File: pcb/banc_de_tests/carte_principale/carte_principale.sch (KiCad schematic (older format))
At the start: 24 parts, among them J1 Arduino_UNO_R3, J2 Conn_02x10_Odd_Even, J3 Conn_01x02, U1 AMS1117-3.3, U2 TSV911AILT

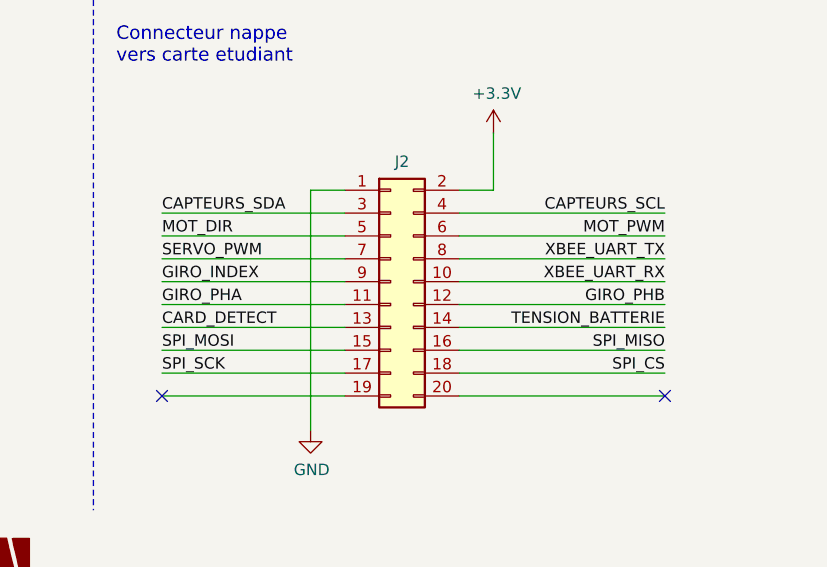
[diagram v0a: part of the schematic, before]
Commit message: Ajout du bus SPI
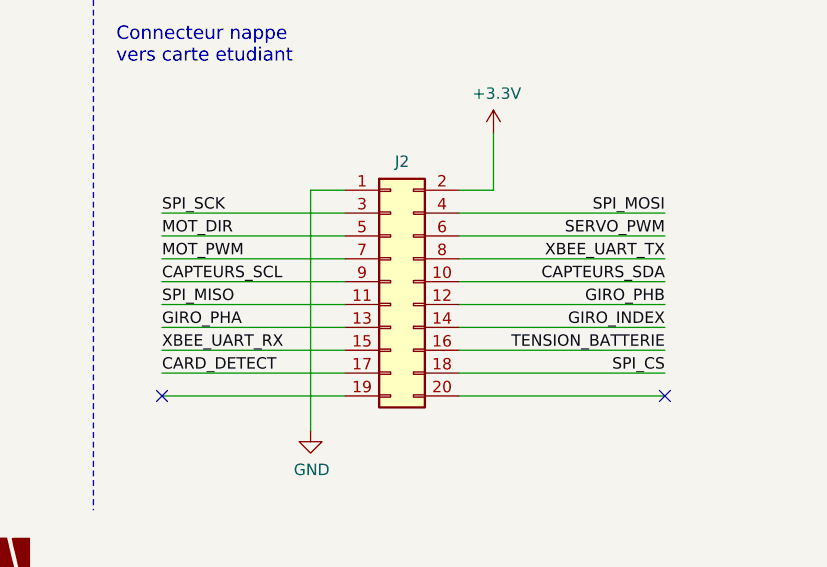
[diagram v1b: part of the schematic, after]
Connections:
- net CAPTEURS_SCL: now also J2.9 (Pin_9); no longer J2.4 (Pin_4)
- net CAPTEURS_SDA: now also J2.10 (Pin_10); no longer J2.3 (Pin_3)
- net CARD_DETECT: now also J2.17 (Pin_17); no longer J2.13 (Pin_13)
- net GIRO_INDEX: now also J2.14 (Pin_14); no longer J2.9 (Pin_9)
- net GIRO_PHA: now also J2.13 (Pin_13); no longer J2.11 (Pin_11)
- net MOT_PWM: now also J2.7 (Pin_7); no longer J2.6 (Pin_6)
- net SERVO_PWM: now also J2.6 (Pin_6); no longer J2.7 (Pin_7)
- net SPI_MISO: now also J2.11 (Pin_11); no longer J2.16 (Pin_16)
- net SPI_MOSI: now also J2.4 (Pin_4); no longer J2.15 (Pin_15)
- net SPI_SCK: now also J2.3 (Pin_3); no longer J2.17 (Pin_17)
- net TENSION_BATTERIE: now also J2.16 (Pin_16); no longer J2.14 (Pin_14)
- net XBEE_UART_RX: now also J2.15 (Pin_15); no longer J2.10 (Pin_10)
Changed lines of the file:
@@
 	1    0    0    -1
 $EndComp
-Text Label 10900 5300 2    50   ~ 0
+Text Label 8700 5400 0    50   ~ 0
 MOT_PWM
 Text Label 8700 5300 0    50   ~ 0
 MOT_DIR
-Text Label 8700 5400 0    50   ~ 0
+Text Label 10900 5300 2    50   ~ 0
 SERVO_PWM
-Text Label 8700 5600 0    50   ~ 0
+Text Label 8700 5700 0    50   ~ 0
 GIRO_PHA
 Text Label 10900 5600 2    50   ~ 0
 GIRO_PHB
+Text Label 10900 5700 2    50   ~ 0
+GIRO_INDEX
+Text Label 10900 5500 2    50   ~ 0
+CAPTEURS_SDA
 Text Label 8700 5500 0    50   ~ 0
-GIRO_INDEX
-Text Label 8700 5200 0    50   ~ 0
-CAPTEURS_SDA
-Text Label 10900 5200 2    50   ~ 0
 CAPTEURS_SCL
 Text Label 10900 5400 2    50   ~ 0
 XBEE_UART_TX
-Text Label 10900 5500 2    50   ~ 0
+Text Label 8700 5800 0    50   ~ 0
 XBEE_UART_RX
 Wire Wire Line
 	9500 5700 8700 5700
-Text Label 10900 5700 2    50   ~ 0
+Text Label 10900 5800 2    50   ~ 0
 TENSION_BATTERIE
 Wire Wire Line
@@
 Wire Wire Line
 	10000 5700 10900 5700
-Text Label 8700 5700 0    50   ~ 0
+Text Label 8700 5900 0    50   ~ 0
 CARD_DETECT
 Wire Wire Line
@@
 NoConn ~ 10900 6000
 NoConn ~ 8700 6000
-Text Label 8700 5800 0    50   ~ 0
+Text Label 10900 5200 2    50   ~ 0
 SPI_MOSI
-Text Label 8700 5900 0    50   ~ 0
+Text Label 8700 5200 0    50   ~ 0
 SPI_SCK
-Text Label 10900 5800 2    50   ~ 0
+Text Label 8700 5600 0    50   ~ 0
 SPI_MISO
 Text Label 10900 5900 2    50   ~ 0

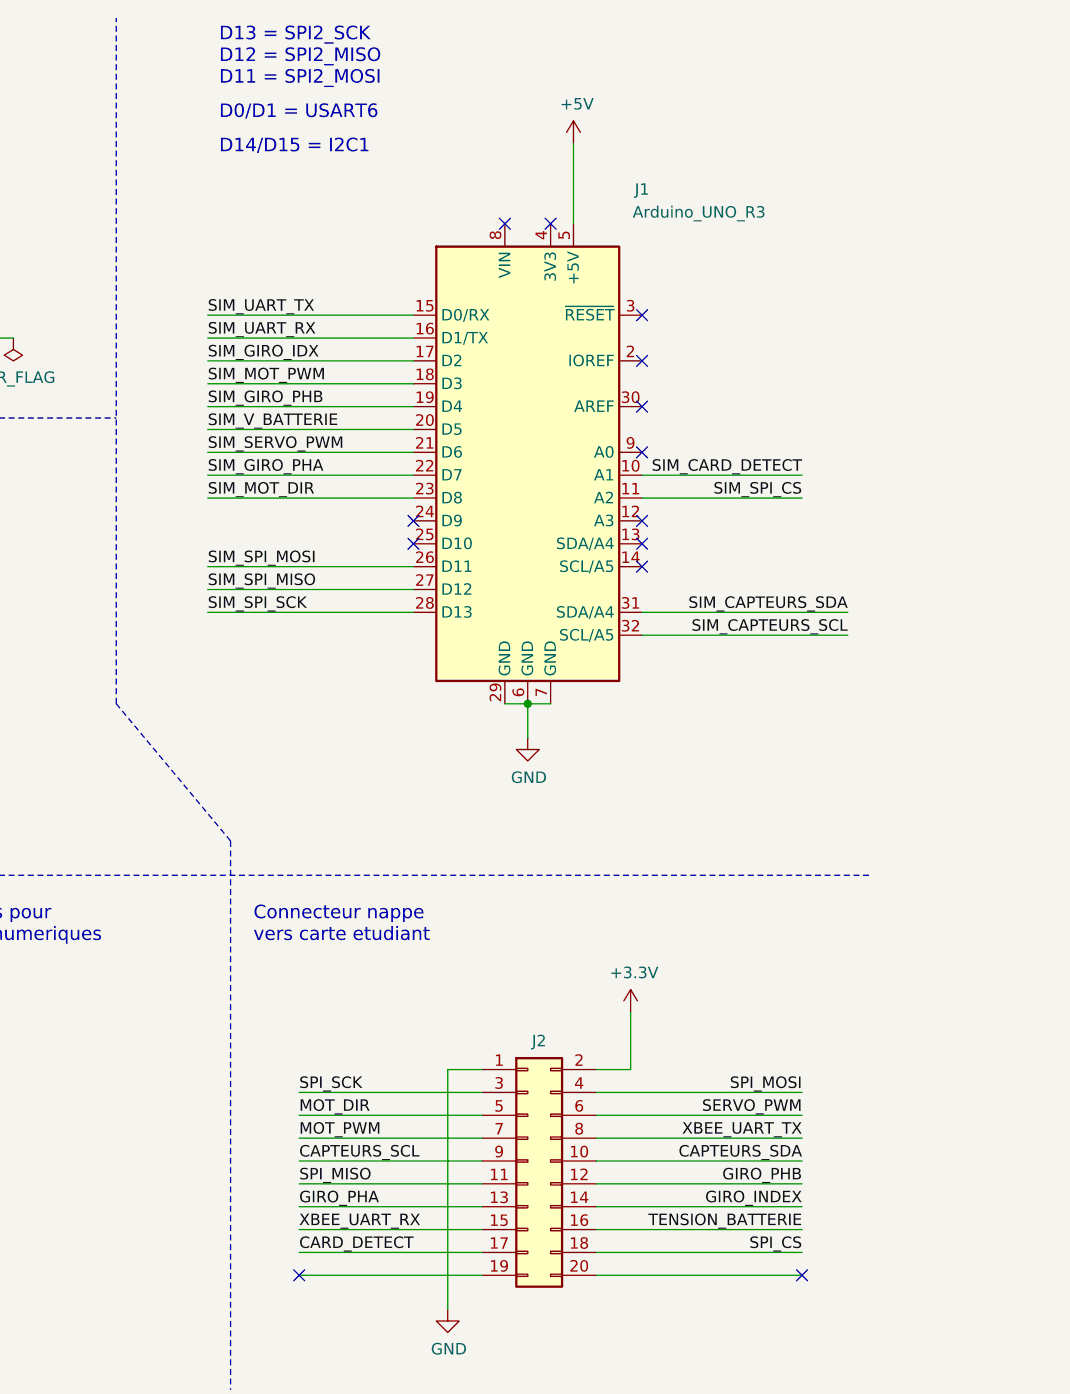
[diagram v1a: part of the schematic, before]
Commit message: * Reorganisation du connecteur de la carte etudiant * premiere version de la carte principale du banc de test * premiere version de la carte vers le connecteur de la carte etudiant
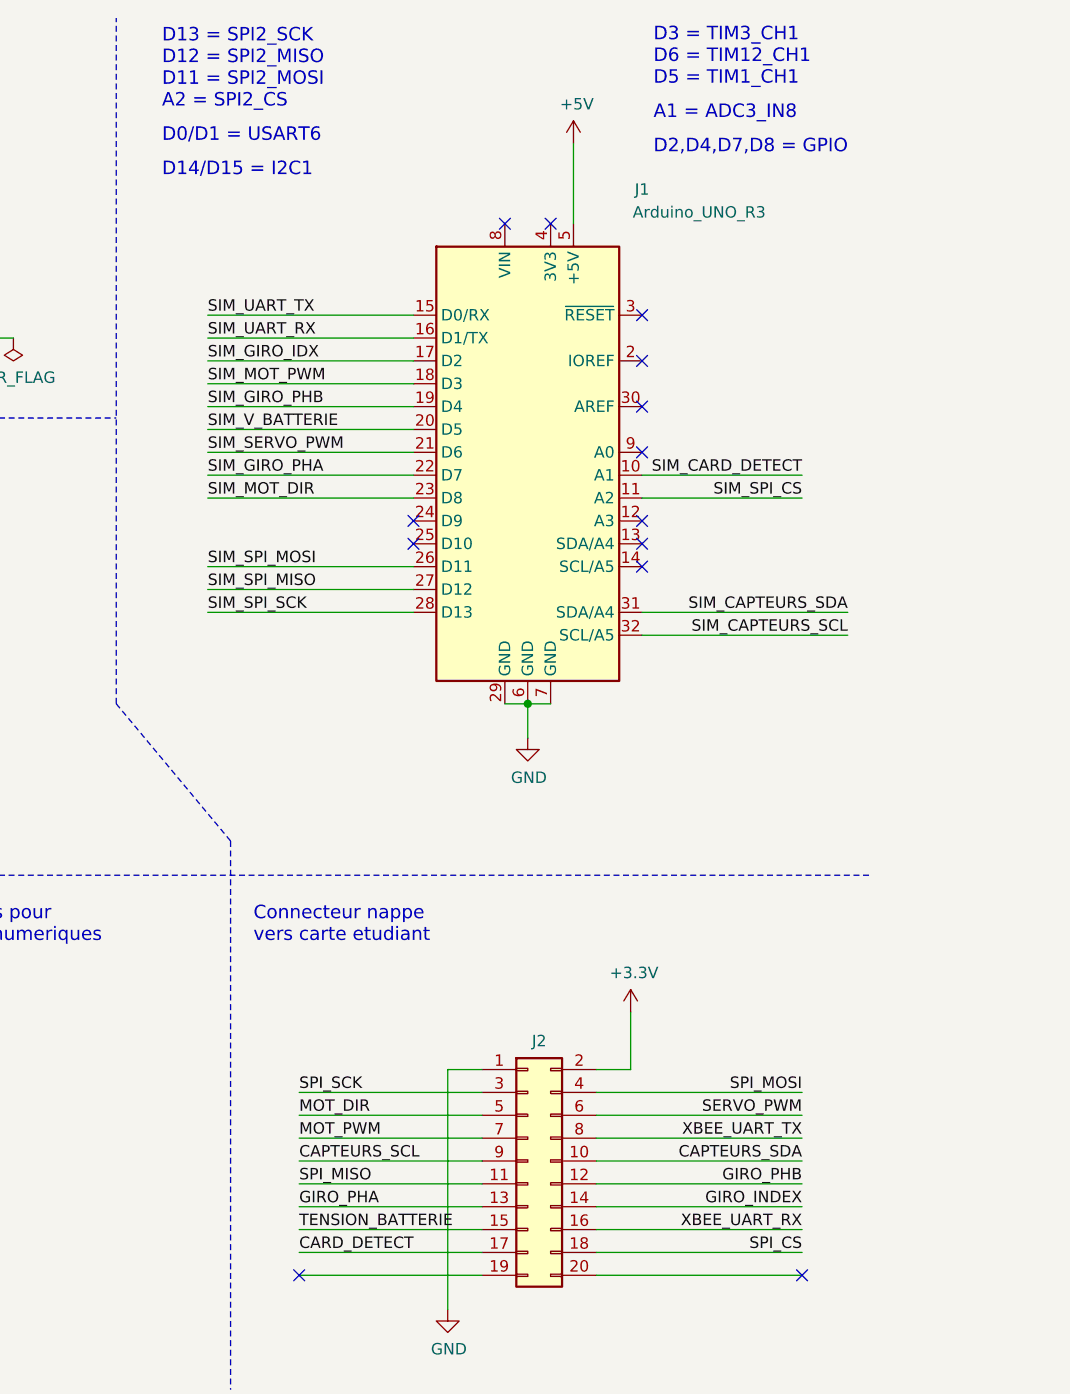
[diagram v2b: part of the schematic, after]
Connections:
- net TENSION_BATTERIE: now also J2.15 (Pin_15); no longer J2.16 (Pin_16)
- net XBEE_UART_RX: now also J2.16 (Pin_16); no longer J2.15 (Pin_15)
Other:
- note added: "A1 = ADC3_IN8"
- note added: "D13 = SPI2_SCK\nD12 = SPI2_MISO\nD11 = SPI2_MOSI\nA2 = SPI2_CS"
- note added: "D2,D4,D7,D8 = GPIO"
- note added: "D3 = TIM3_CH1\nD6 = TIM12_CH1\nD5 = TIM1_CH1"
- note removed: "D13 = SPI2_SCK\nD12 = SPI2_MISO\nD11 = SPI2_MOSI"
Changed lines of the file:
@@
 Wire Notes Line
 	7900 3500 7900 500
-Text Notes 8350 800  0    59   ~ 0
-D13 = SPI2_SCK\nD12 = SPI2_MISO\nD11 = SPI2_MOSI
-Text Notes 8350 950  0    59   ~ 0
+Text Notes 8100 900  0    59   ~ 0
+D13 = SPI2_SCK\nD12 = SPI2_MISO\nD11 = SPI2_MOSI\nA2 = SPI2_CS
+Text Notes 8100 1050 0    59   ~ 0
 D0/D1 = USART6
-Text Notes 8350 1100 0    59   ~ 0
+Text Notes 8100 1200 0    59   ~ 0
 D14/D15 = I2C1
 $Comp
@@
 Text Label 10900 5400 2    50   ~ 0
 XBEE_UART_TX
+Text Label 10900 5800 2    50   ~ 0
+XBEE_UART_RX
+Wire Wire Line
+	9500 5700 8700 5700
 Text Label 8700 5800 0    50   ~ 0
-XBEE_UART_RX
-Wire Wire Line
-	9500 5700 8700 5700
-Text Label 10900 5800 2    50   ~ 0
 TENSION_BATTERIE
 Wire Wire Line
@@
 F25 "SIM_SPI_CS" O R 4550 6500 50
 $EndSheet
+Text Notes 10250 800  0    59   ~ 0
+D3 = TIM3_CH1\nD6 = TIM12_CH1\nD5 = TIM1_CH1
+Text Notes 10250 950  0    59   ~ 0
+A1 = ADC3_IN8
+Text Notes 10250 1100 0    59   ~ 0
+D2,D4,D7,D8 = GPIO
 $EndSCHEMATC
